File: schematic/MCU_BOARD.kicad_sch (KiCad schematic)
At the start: 82 parts, among them J2 Speaker_Conn_01x02, J3 Barrel_Jack_Switch, J4 Conn_01x27, Q1 2N3904, Q2 2N3904, Q3 2N3904, Q4 2N3904, Q5 2N3904, U5 LM386, U6 74HC4051, U7 AT89S51-24PU, U9 SN74HC4060N, Y1 32.768Khz, Y2 12Mhz

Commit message: changed cap values to fix issues with clock crystial, was off by +2 hz
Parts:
- C1: value 12pF -> 47pF
- C2: value 5-20pF -> 6-30pF
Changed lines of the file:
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@@
     (in_bom yes) (on_board yes)
     (property "Reference" "C2" (id 0) (at 34.925 159.385 90))
-    (property "Value" "5-20pF" (id 1) (at 34.925 156.845 90))
+    (property "Value" "6-30pF" (id 1) (at 34.925 156.845 90))
     (property "Footprint" "Capacitor_THT:C_Rect_L7.0mm_W6.5mm_P5.00mm" (id 2) (at 34.925 152.4 0)
       (effects (font (size 1.27 1.27)) hide)
@@
     (in_bom yes) (on_board yes)
     (property "Reference" "C1" (id 0) (at 34.925 138.43 90))
-    (property "Value" "12pF" (id 1) (at 34.925 140.97 90))
+    (property "Value" "47pF" (id 1) (at 34.925 140.97 90))
     (property "Footprint" "Capacitor_THT:C_Disc_D4.3mm_W1.9mm_P5.00mm" (id 2) (at 38.735 143.8148 0)
       (effects (font (size 1.27 1.27)) hide)

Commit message: tweaked the schematic, now the trimmer cap + start value adds up to the other cap of 47 pf for balance.
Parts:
- C26: value 12pF -> 18pF
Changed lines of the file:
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@@
     (in_bom yes) (on_board yes)
     (property "Reference" "C26" (id 0) (at 34.925 170.815 90))
-    (property "Value" "12pF" (id 1) (at 34.925 168.275 90))
+    (property "Value" "18pF" (id 1) (at 34.925 168.275 90))
     (property "Footprint" "Capacitor_THT:C_Disc_D4.3mm_W1.9mm_P5.00mm" (id 2) (at 31.115 165.4302 0)
       (effects (font (size 1.27 1.27)) hide)

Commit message: added padding resistor to halve the speaker volume and deal with some noise issues in some units. Noise is originating from the 7 segment LED data lines. It runs at about 1khz so this makes sense, will try some software fixes in the future.
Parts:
- added R19: 8R_OPT, Resistor_THT:R_Axial_DIN0414_L11.9mm_D4.5mm_P15.24mm_Horizontal, symbol Device:R
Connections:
- net at C15.2: now also R19.2; no longer J2.2 (Pin_2)
- new net: J2.2 (Pin_2), R19.1
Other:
- moved on the sheet: J2
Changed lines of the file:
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@@
+    (stroke (width 0) (type default) (color 0 0 0 0))
+  )
+  (wire (pts (xy 248.92 38.1) (xy 256.54 38.1))
     (stroke (width 0) (type default) (color 0 0 0 0))
   )
@@
     (pin "2")
   )
+  (symbol (lib_id "Device:R") (at 252.73 40.64 270) (unit 1)
+    (in_bom yes) (on_board yes)
+    (property "Reference" "R19" (id 0) (at 251.46 34.925 90)
+      (effects (font (size 1.27 1.27)) (justify left))
+    )
+    (property "Value" "8R_OPT" (id 1) (at 250.19 36.83 90)
+      (effects (font (size 1.27 1.27)) (justify left))
+    )
+    (property "Footprint" "Resistor_THT:R_Axial_DIN0414_L11.9mm_D4.5mm_P15.24mm_Horizontal" (id 2) (at 252.73 38.862 90)
+      (effects (font (size 1.27 1.27)) hide)
+    )
+    (property "Datasheet" "~" (id 3) (at 252.73 40.64 0)
+      (effects (font (size 1.27 1.27)) hide)
+    )
+    (pin "1")
+    (pin "2")
+  )
   (symbol (lib_id "power:GND") (at 55.88 160.02 0) (mirror y) (unit 1)
     (in_bom yes) (on_board yes)
@@
     (pin "1")
   )
-  (symbol (lib_id "Connector_Generic:Conn_01x02") (at 254 38.1 0) (unit 1)
-    (in_bom yes) (on_board yes)
-    (property "Reference" "J2" (id 0) (at 254 46.99 0))
-    (property "Value" "Speaker_Conn_01x02" (id 1) (at 249.555 44.45 0))
-    (property "Footprint" "Connector_Molex:Molex_KK-254_AE-6410-02A_1x02_P2.54mm_Vertical" (id 2) (at 254 38.1 0)
-      (effects (font (size 1.27 1.27)) hide)
-    )
-    (property "Datasheet" "~" (id 3) (at 254 38.1 0)
-      (effects (font (size 1.27 1.27)) hide)
-    )
+  (symbol (lib_id "Connector_Generic:Conn_01x02") (at 261.62 38.1 0) (unit 1)
+    (in_bom yes) (on_board yes)
+    (property "Reference" "J2" (id 0) (at 261.62 46.99 0))
+    (property "Value" "Speaker_Conn_01x02" (id 1) (at 255.27 44.45 0))
+    (property "Footprint" "Connector_Molex:Molex_KK-254_AE-6410-02A_1x02_P2.54mm_Vertical" (id 2) (at 261.62 38.1 0)
+      (effects (font (size 1.27 1.27)) hide)
+    )
+    (property "Datasheet" "~" (id 3) (at 261.62 38.1 0)
+      (effects (font (size 1.27 1.27)) hide)
+    )

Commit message: mit license update
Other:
- company: JDC -> sparkletron
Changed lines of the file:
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@@
     (date "2022-12-11")
     (rev "v1.0")
-    (company "JDC")
+    (company "sparkletron")
+    (comment 1 "Jay Convertino")
+    (comment 2 "MIT License")
   )
   (junction (at 46.355 27.94) (diameter 0) (color 0 0 0 0)

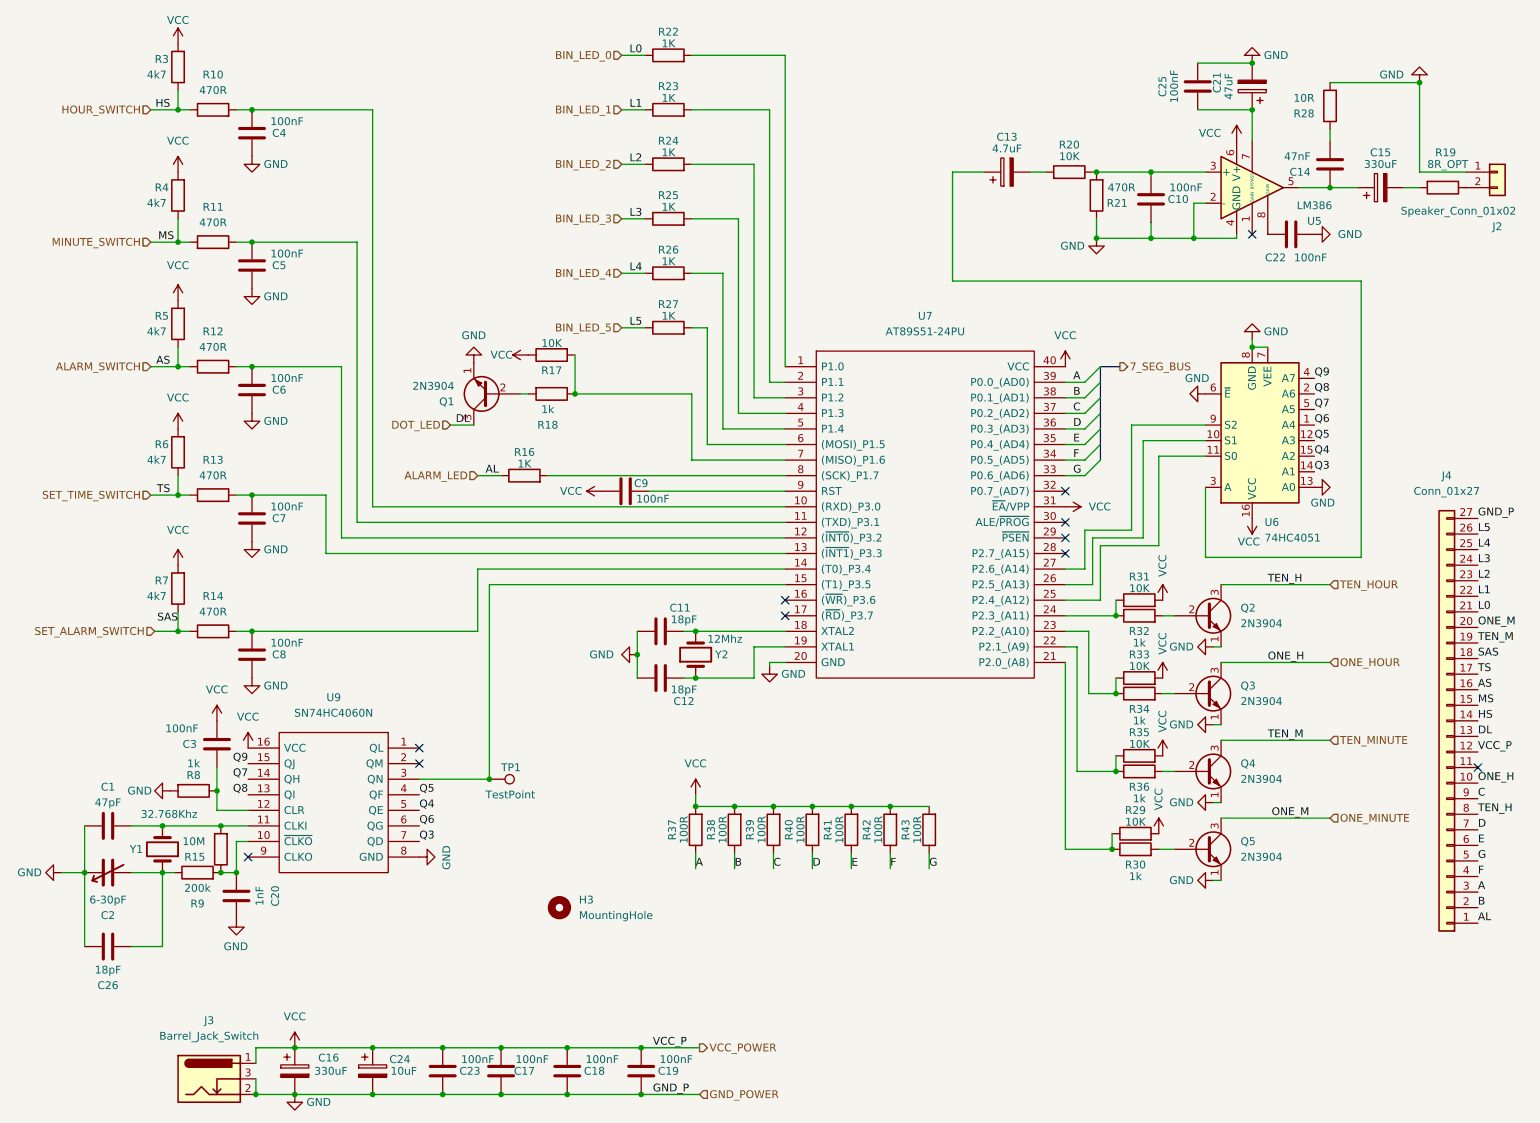
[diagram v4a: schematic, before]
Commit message: bad state, but wanted to document changes to the v1 cap values. Need to fix PCB, it got messed up for some odd reason.
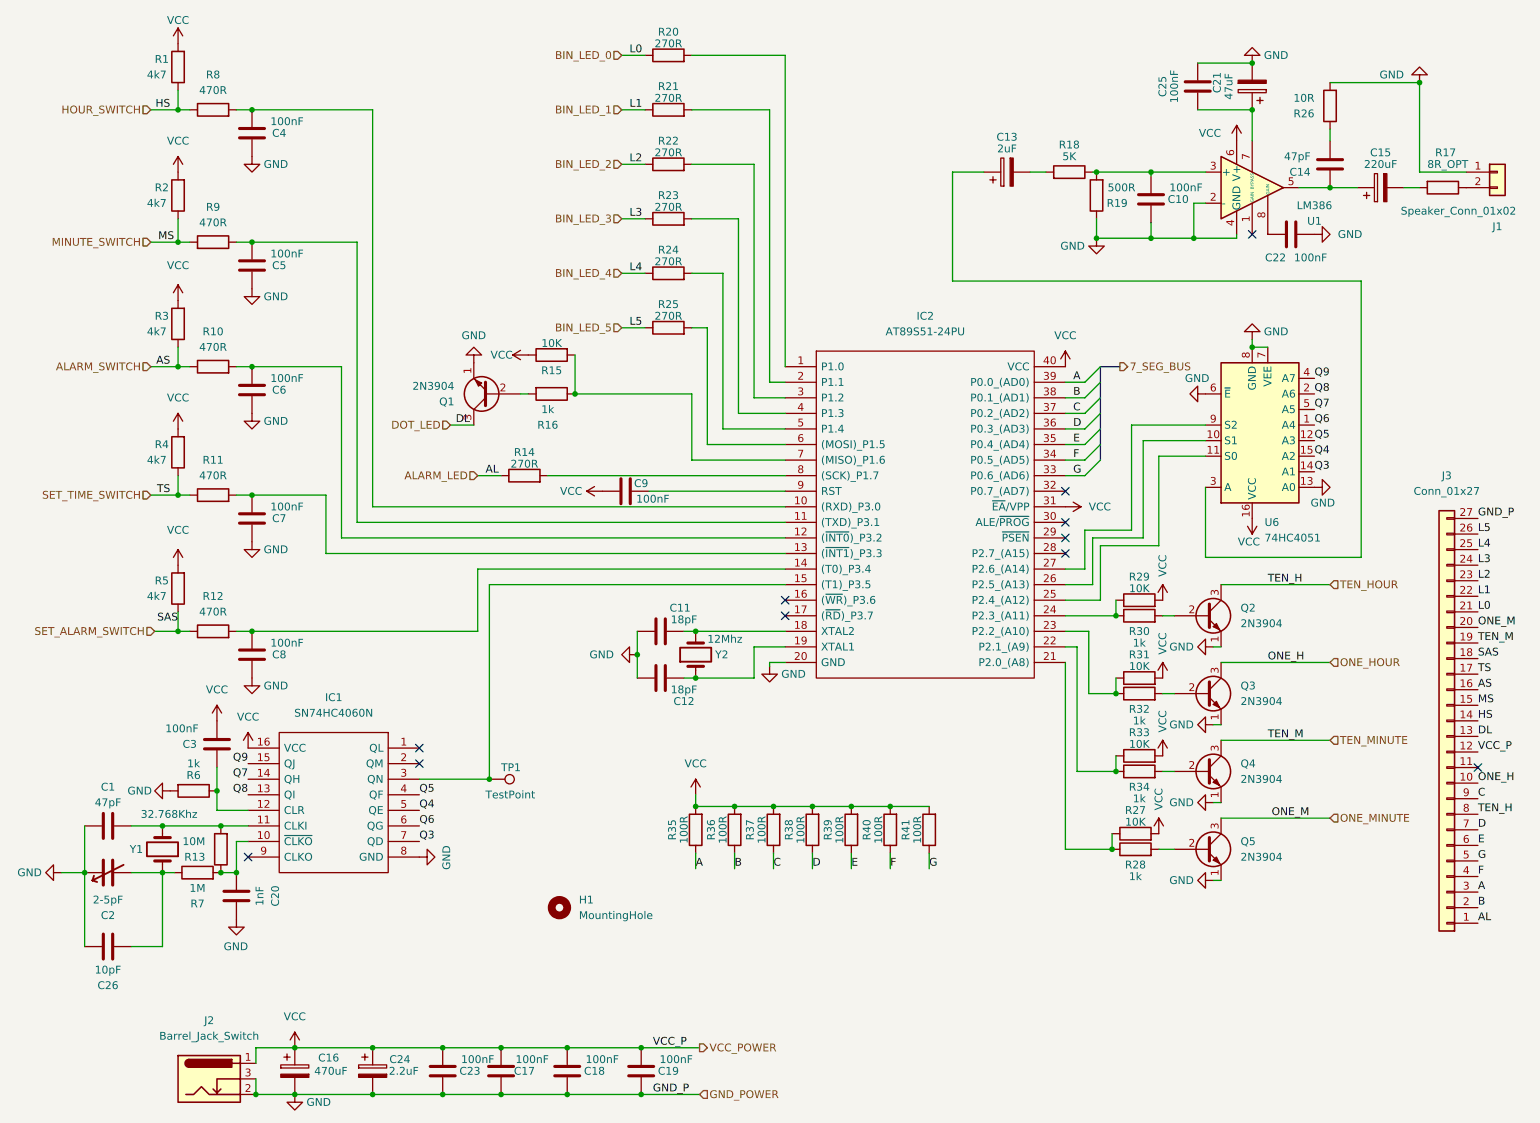
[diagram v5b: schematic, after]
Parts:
- C1: footprint Capacitor_THT:C_Disc_D4.3mm_W1.9mm_P5.00mm -> Capacitor_THT:C_Disc_D3.0mm_W1.6mm_P2.50mm
- C13: value 4.7uF -> 2uF
- C14: value 47nF -> 47pF; footprint Capacitor_THT:C_Disc_D4.3mm_W1.9mm_P5.00mm -> Capacitor_THT:C_Disc_D3.0mm_W2.0mm_P2.50mm
- C15: value 330uF -> 220uF; footprint Capacitor_THT:CP_Radial_D6.3mm_P2.50mm -> Capacitor_THT:CP_Radial_D10.0mm_P5.00mm_P7.50mm
- C16: value 330uF -> 470uF; footprint Capacitor_THT:CP_Radial_D6.3mm_P2.50mm -> Capacitor_THT:CP_Radial_D10.0mm_P5.00mm_P7.50mm
- C2: value 6-30pF -> 2-5pF; footprint Capacitor_THT:C_Rect_L7.0mm_W6.5mm_P5.00mm -> Capacitor_THT:C_Rect_L10.0mm_W5.0mm_P5.00mm_P7.50mm
- C24: value 10uF -> 2.2uF
- C26: value 18pF -> 10pF
- R14: renamed from R16; value 1K -> 270R
- R18: renamed from R20; value 10K -> 5K
- R19: renamed from R21; value 470R -> 500R
- R20: renamed from R22; value 1K -> 270R
- R21: renamed from R23; value 1K -> 270R
- R22: renamed from R24; value 1K -> 270R
- R23: renamed from R25; value 1K -> 270R
- R24: renamed from R26; value 1K -> 270R
- R25: renamed from R27; value 1K -> 270R
- R7: renamed from R9; value 200k -> 1M
- renumbered H3 to H1, U9 to IC1, U7 to IC2, J2 to J1, J3 to J2, J4 to J3, R3 to R1, R12 to R10, R13 to R11, R14 to R12, R15 to R13, R17 to R15, R18 to R16, R19 to R17, R4 to R2, R28 to R26, R29 to R27, R30 to R28, R31 to R29, R5 to R3, R32 to R30, R33 to R31, R34 to R32, R35 to R33, R36 to R34, R37 to R35, R38 to R36, R39 to R37, R40 to R38, R41 to R39, R6 to R4, R42 to R40, R43 to R41, R7 to R5, R8 to R6, R10 to R8, R11 to R9, U5 to U1

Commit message: added resistor from input to bypass of lm386. When the alarm is off the input is ground, this reduces noise issues to about nothing. Updated PCB.
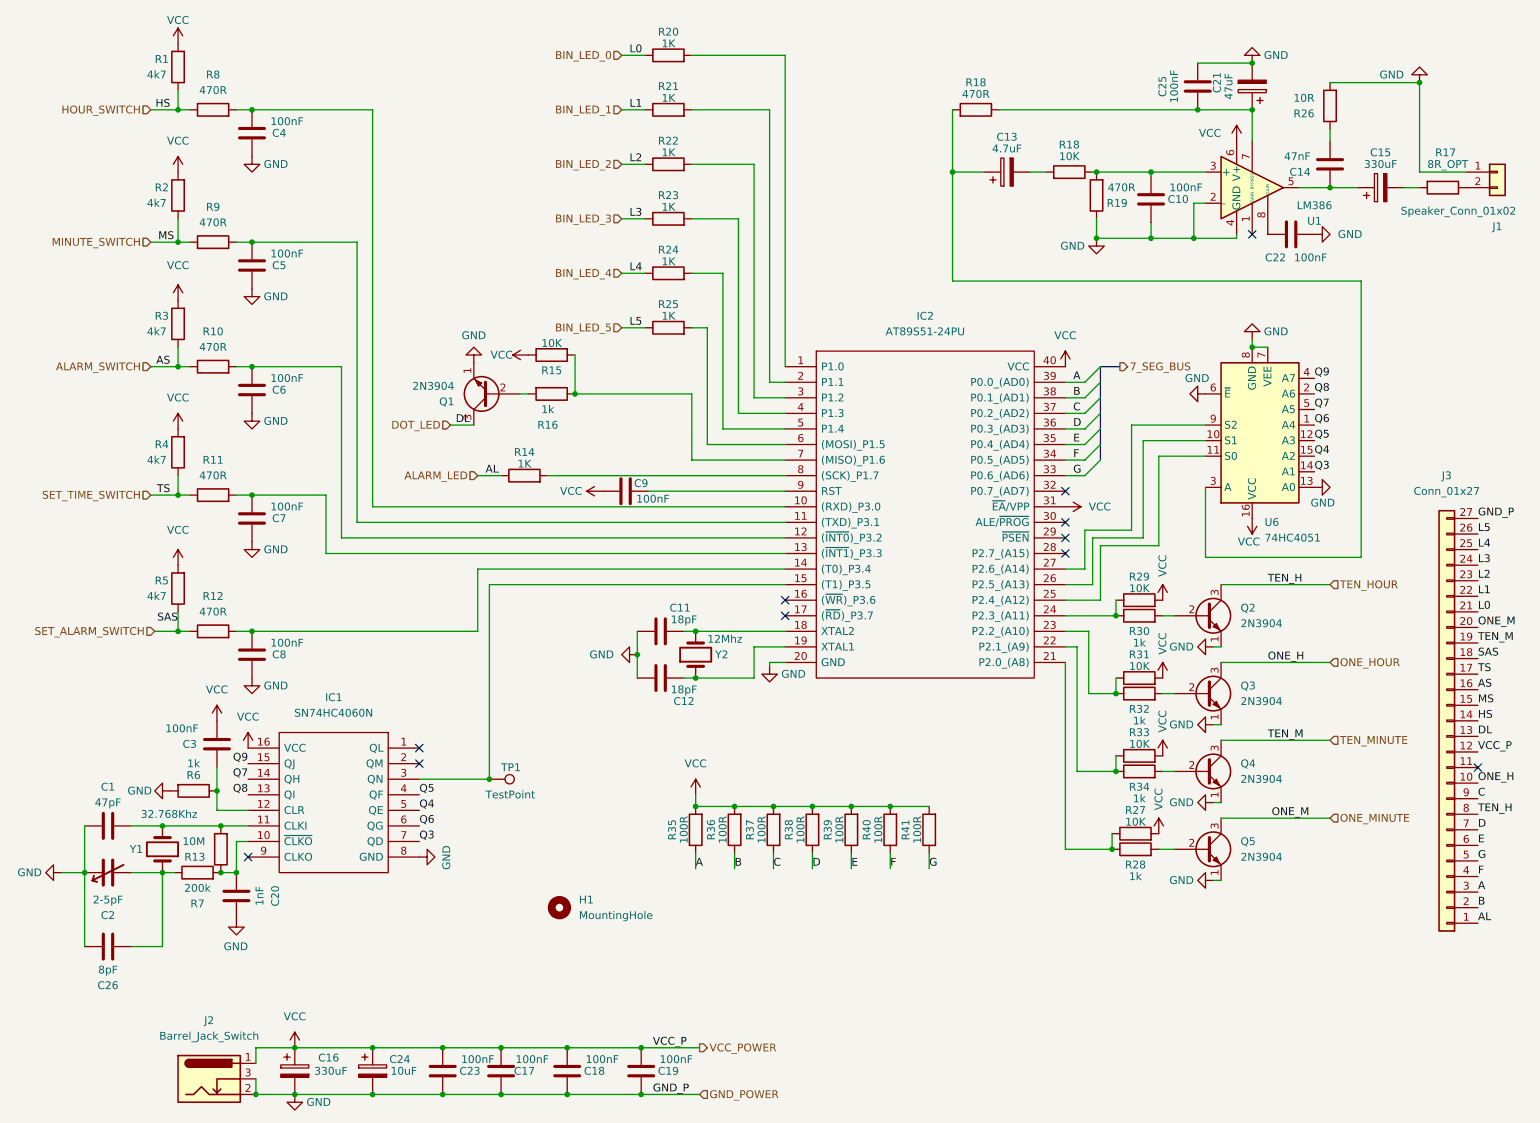
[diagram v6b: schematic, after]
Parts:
- added R18: 470R, Resistor_THT:R_Axial_DIN0207_L6.3mm_D2.5mm_P7.62mm_Horizontal, symbol Device:R
- C1: footprint Capacitor_THT:C_Disc_D3.0mm_W1.6mm_P2.50mm -> Capacitor_THT:C_Disc_D4.3mm_W1.9mm_P5.00mm
- C13: value 2uF -> 4.7uF
- C14: value 47pF -> 47nF; footprint Capacitor_THT:C_Disc_D3.0mm_W2.0mm_P2.50mm -> Capacitor_THT:C_Disc_D4.3mm_W1.9mm_P5.00mm
- C15: value 220uF -> 330uF; footprint Capacitor_THT:CP_Radial_D10.0mm_P5.00mm_P7.50mm -> Capacitor_THT:CP_Radial_D6.3mm_P2.50mm
- C16: value 470uF -> 330uF; footprint Capacitor_THT:CP_Radial_D10.0mm_P5.00mm_P7.50mm -> Capacitor_THT:CP_Radial_D6.3mm_P2.50mm
- C2: footprint Capacitor_THT:C_Rect_L10.0mm_W5.0mm_P5.00mm_P7.50mm -> Capacitor_THT:C_Rect_L7.0mm_W6.5mm_P5.00mm
- C24: value 2.2uF -> 10uF
- C26: value 10pF -> 8pF
- R14, R20, R21, R22, R23, R24, R25: value 270R -> 1K
- R18: value 5K -> 10K
- R19: value 500R -> 470R
- R7: value 1M -> 200k
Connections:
- net at C13.1, U6.3 (A): now also R18.2
- net at C21.1, C25.1, U1.7 (BYPASS): now also R18.1

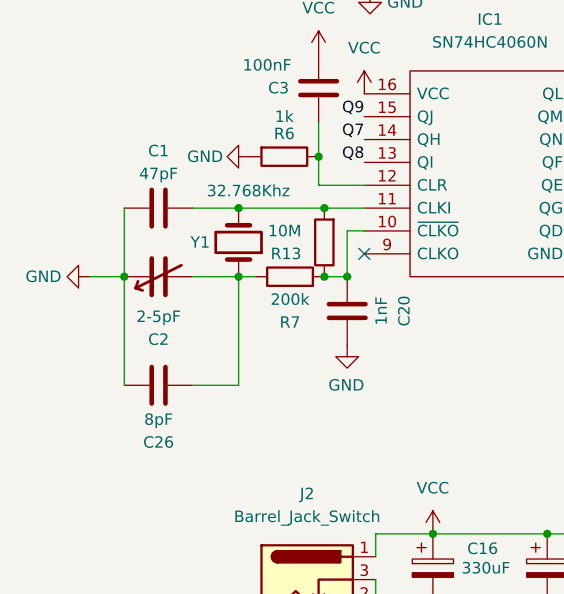
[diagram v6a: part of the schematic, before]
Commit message: adjusted cap values for best possible +/- 3 hz adjustment around 2048 clock output. This produces the best clock so far and allows for finer tuning at the lower frequencies.
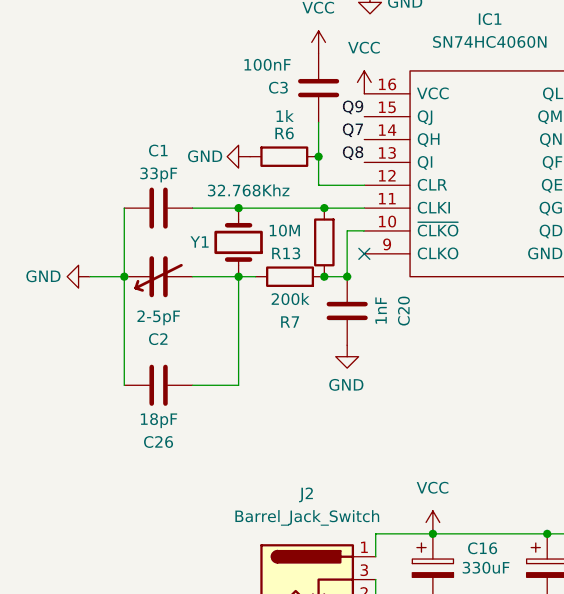
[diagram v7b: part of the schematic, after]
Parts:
- C1: value 47pF -> 33pF
- C26: value 8pF -> 18pF
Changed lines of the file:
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@@
       (effects (font (size 1.27 1.27)))
     )
-    (property "Value" "8pF" (at 34.925 168.275 90)
+    (property "Value" "18pF" (at 34.925 168.275 90)
       (effects (font (size 1.27 1.27)))
     )
@@
       (effects (font (size 1.27 1.27)))
     )
-    (property "Value" "47pF" (at 34.925 140.97 90)
-      (effects (font (size 1.27 1.27)))
-    )
+    (property "Value" "33pF" (at 34.925 140.97 90)
+      (effects (font (size 1.27 1.27)))
+    )
